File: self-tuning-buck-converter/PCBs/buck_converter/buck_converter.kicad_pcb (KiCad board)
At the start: 2 copper layers, 42 parts, among them Q1 NMOS, U1 AMP from lab, U2 LM7322, U3 LT1999-50, U4 LD1117V50, U6 ESP32-DEVKITC-32D, U7 IR2125, U8 MAX11644

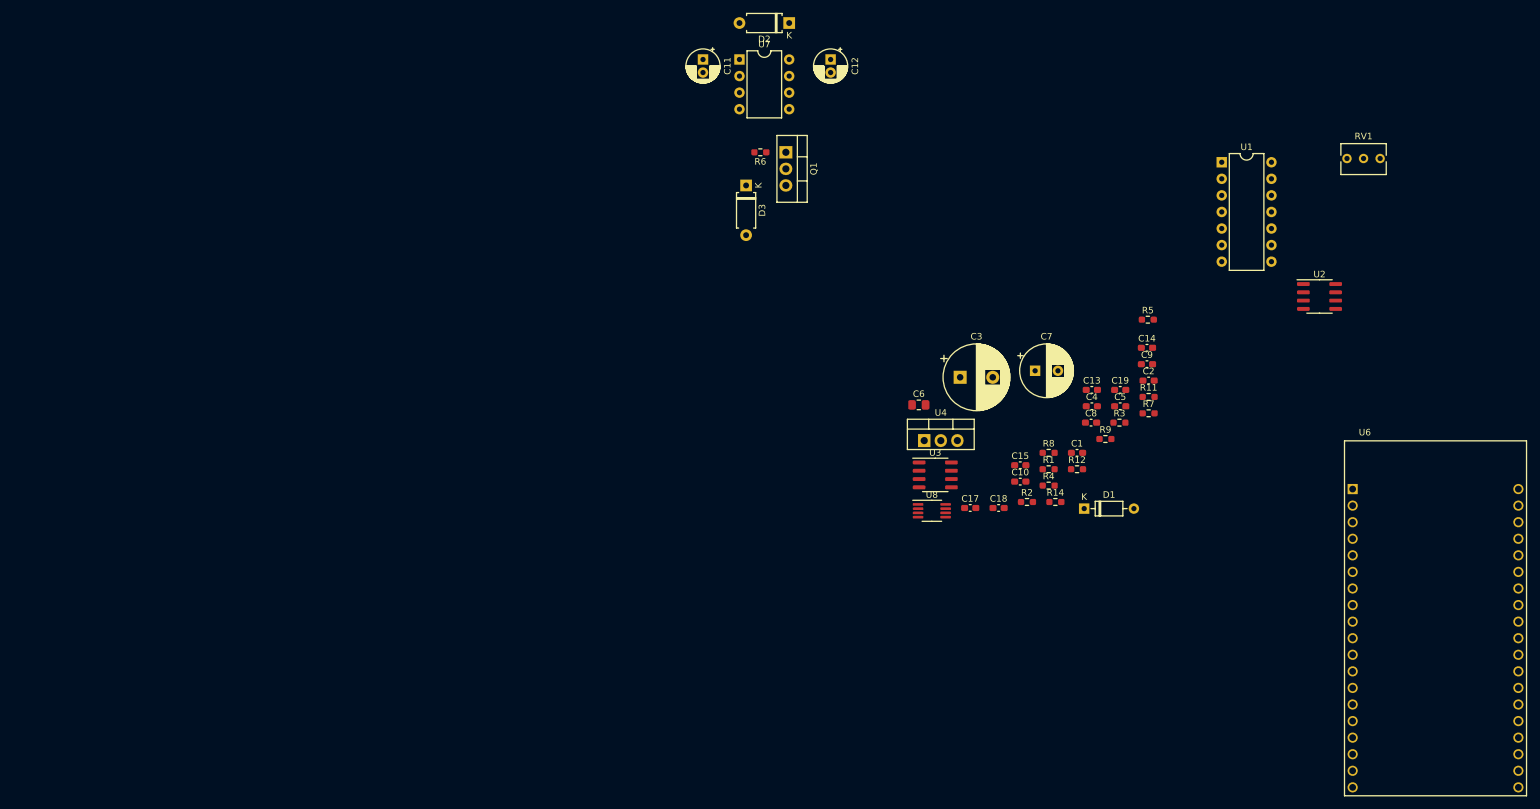
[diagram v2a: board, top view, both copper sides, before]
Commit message: begin and almost complete the PCB design of the buck converter:
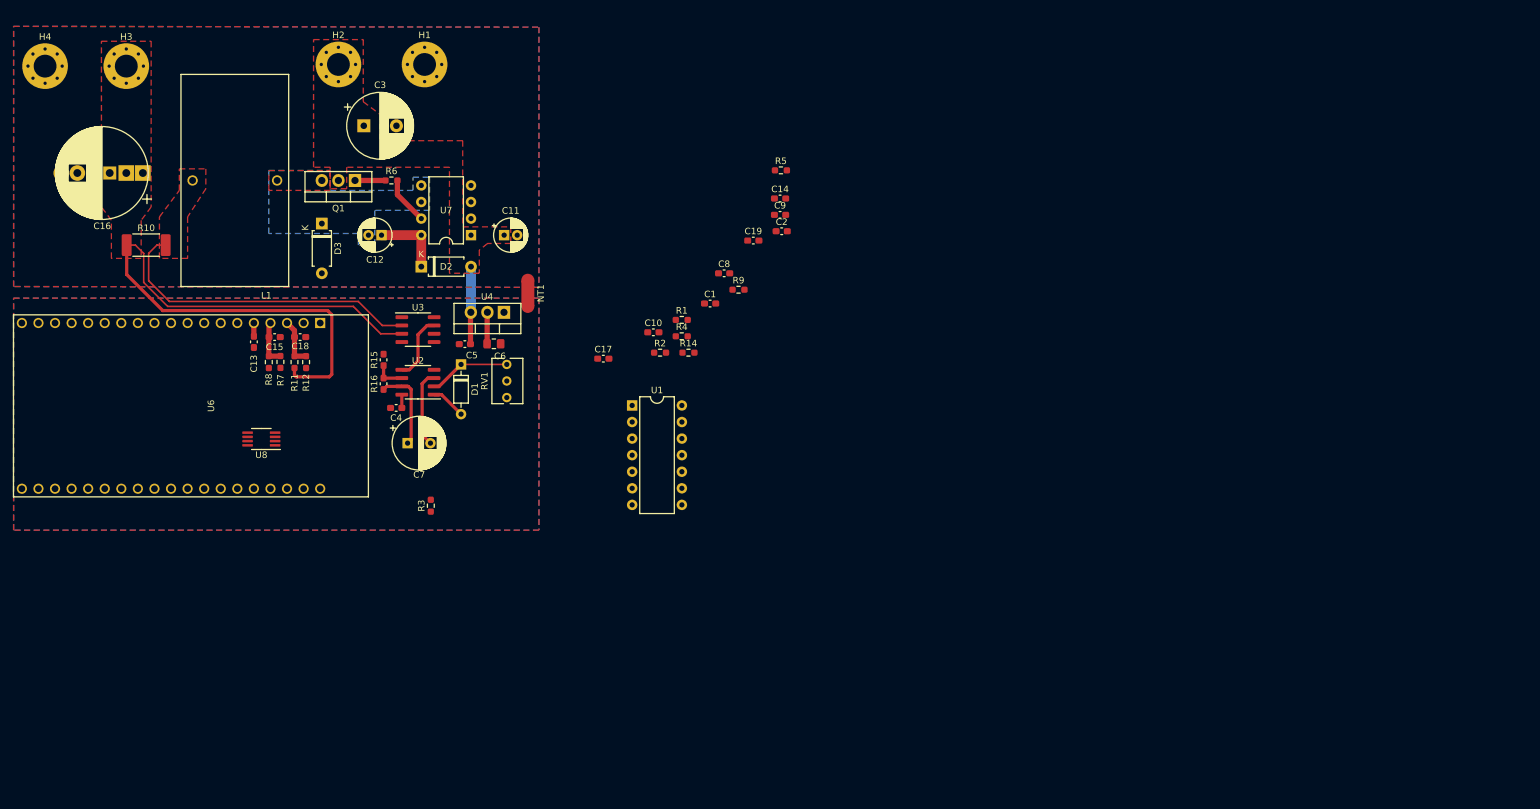
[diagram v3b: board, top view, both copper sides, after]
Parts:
- added C16: 470u 50V, multi_capacitor:multi_cap, F.Cu at (-204.3, -111.5)
- added H1: GND_IN, MountingHole:MountingHole_3.5mm_Pad_Via, F.Cu at (-154.9, -128.0)
- added H2: VCC_IN, MountingHole:MountingHole_3.5mm_Pad_Via, F.Cu at (-168.1, -128.0)
- added H3: LOAD +, MountingHole:MountingHole_3.5mm_Pad_Via, F.Cu at (-200.7, -127.8)
- added H4: LOAD -, MountingHole:MountingHole_3.5mm_Pad_Via, F.Cu at (-213.1, -127.8)
- added L1: L, IND_HCTI-150-5.0:IND_HCTI-150-5.0, F.Cu at (-184.0, -110.2)
- added NT1: Net-Tie_2, NetTie:NetTie-2_SMD_Pad2.0mm, F.Cu at (-139.1, -92.9)
- added R10: 60m, Resistor_SMD:R_2512_6332Metric_Pad1.52x3.35mm_HandSolder, F.Cu at (-197.6, -100.3)
- added R15: 10k, Resistor_SMD:R_0603_1608Metric_Pad1.05x0.95mm_HandSolder, F.Cu at (-161.2, -82.7)
- added R16: 10k, Resistor_SMD:R_0603_1608Metric_Pad1.05x0.95mm_HandSolder, F.Cu at (-161.2, -79.1)
- U2: value LM7322 -> OPA2830
- moved U6 193.5 mm to (-190.7, -75.7), turned to 270 degrees
- moved U2 138.8 mm to (-156.0, -79.3), turned to 180 degrees
- moved RV1 137.5 mm to (-142.3, -82.0), turned to 90 degrees
- moved R7 133.3 mm to (-177.0, -82.4), turned to 90 degrees
- moved R11 131.0 mm to (-174.9, -82.4), turned to 90 degrees
- moved C13 128.6 mm to (-181.1, -85.5), turned to 90 degrees
- moved R8 120.3 mm to (-178.8, -82.4), turned to 270 degrees
- moved R12 119.3 mm to (-173.1, -82.4), turned to 270 degrees
- moved C15 116.0 mm to (-177.9, -86.2), turned to 180 degrees
- moved C18 110.2 mm to (-174.0, -86.2), turned to 180 degrees
- moved C4 106.6 mm to (-159.3, -75.4)
- moved R3 106.3 mm to (-154.0, -60.4), turned to 90 degrees
- moved U8 103.4 mm to (-180.0, -70.6), turned to 180 degrees
- moved C5 100.9 mm to (-148.8, -85.2), turned to 180 degrees
- moved C3 99.2 mm to (-164.3, -118.6)
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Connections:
- C7 pad 1: Sense_out -> Sense_ripple
- R5 pad 2: Sense_out -> Sense_avg
- RV1 pad 3: Net-(RV1-Pad3) -> (no net)
- U1 pad 2: Net-(R1-Pad2) -> V_ref
- U1 pad 3: V_ref -> Net-(R1-Pad2)
- U1 pad 5: Pk_voltage -> Net-(C9-Pad2)
- U1 pad 6: Net-(C9-Pad2) -> Pk_voltage
- U2 pad 5: (no net) -> Sense_avg
- U2 pad 6: (no net) -> Net-(R15-Pad1)
- U2 pad 7: (no net) -> Sense_ripple
- U3 pad 7: Sense_out -> Sense_avg
- U3 pad 8: Net-(U3-Pad8) -> (no net)
- U6 pad 1: Net-(U6-Pad1) -> (no net)
- U6 pad 12: Net-(U6-Pad12) -> (no net)
- U6 pad 13: Net-(U6-Pad13) -> (no net)
- U6 pad 15: Net-(U6-Pad15) -> (no net)
- U6 pad 16: Net-(U6-Pad16) -> (no net)
- U6 pad 17: Net-(U6-Pad17) -> (no net)
- U6 pad 18: Net-(U6-Pad18) -> (no net)
- U6 pad 2: Net-(U6-Pad2) -> (no net)
- U6 pad 21: Net-(U6-Pad21) -> (no net)
- U6 pad 22: Net-(U6-Pad22) -> (no net)
- U6 pad 23: Net-(U6-Pad23) -> (no net)
- U6 pad 24: Net-(U6-Pad24) -> (no net)
- U6 pad 25: Net-(U6-Pad25) -> (no net)
- U6 pad 27: Net-(U6-Pad27) -> (no net)
- U6 pad 28: Net-(U6-Pad28) -> (no net)
- U6 pad 29: Net-(U6-Pad29) -> (no net)
- U6 pad 30: Net-(U6-Pad30) -> (no net)
- U6 pad 31: Net-(U6-Pad31) -> (no net)
- U6 pad 32: Net-(U6-Pad32) -> (no net)
- U6 pad 33: Net-(U6-Pad33) -> (no net)
- U6 pad 34: Net-(U6-Pad34) -> (no net)
- U6 pad 35: Net-(U6-Pad35) -> (no net)
- U6 pad 36: Net-(U6-Pad36) -> (no net)
- U6 pad 37: Net-(U6-Pad37) -> (no net)
- U6 pad 38: Net-(U6-Pad38) -> (no net)
- U6 pad 6: Net-(U6-Pad6) -> (no net)
- U6 pad 7: Net-(U6-Pad7) -> (no net)
- U6 pad 8: Net-(U6-Pad8) -> (no net)
- U7 pad 3: Net-(U7-Pad3) -> (no net)
- U8 pad 3: Net-(U8-Pad3) -> (no net)
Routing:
- net V_load: track 0.00 -> 105.1 mm
- net /sen_p: track 0.00 -> 49.0 mm
- net +12V: track 0.00 -> 13.9 mm
- net Sense_ripple: track 0.00 -> 13.1 mm
- net Net-(D1-Pad1): track 0.00 -> 12.5 mm
- net Net-(C7-Pad2): track 0.00 -> 11.8 mm
- net Net-(C12-Pad1): track 0.00 -> 10.9 mm
- net Sense_avg: track 0.00 -> 10.1 mm
- net load_sense: track 0.00 -> 7.40 mm
- net Net-(R6-Pad2): track 0.00 -> 7.36 mm
- net V_supply: track 0.00 -> 6.97 mm
- net Net-(D1-Pad2): track 0.00 -> 5.37 mm
- net +5V: track 0.00 -> 4.84 mm
- net Net-(R15-Pad1): track 0.00 -> 4.71 mm
- net Net-(Q1-Pad1): track 0.00 -> 4.68 mm
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- added copper zone on F.Cu, net +12V
- added copper zone on F.Cu, net /sen_p
- added copper zone on B.Cu, net GND
- added copper zone on F.Cu, net GND
- added copper zone on B.Cu, net GNDD
- added copper zone on F.Cu, net GNDD
- added copper zone on B.Cu, net Net-(C12-Pad2)
- added copper zone on F.Cu, net Net-(C12-Pad2)
- added copper zone on F.Cu, net V_load

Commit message: completed the PCB design
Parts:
- added R13: 16k, Resistor_SMD:R_0603_1608Metric_Pad0.98x0.95mm_HandSolder, F.Cu at (-194.2, -87.7)
- C8: value 0.1u 16V -> 1u 16V
- IN +: renamed from H2
- IN -: renamed from H1
- OUT  -: renamed from H4
- OUT +: renamed from H3
- U1: value AMP from lab -> TLO84CN
- moved C2 106.9 mm to (-205.7, -85.1), turned to 270 degrees
- moved R5 105.2 mm to (-201.7, -83.8), turned to 270 degrees
- moved C14 103.4 mm to (-192.6, -60.6), turned to 90 degrees
- moved C9 100.5 mm to (-196.5, -75.6), turned to 90 degrees
- moved R9 90.2 mm to (-190.9, -60.7), turned to 270 degrees
- moved C8 87.2 mm to (-195.8, -87.7), turned to 90 degrees
- moved C19 87.0 mm to (-184.0, -65.4), turned to 270 degrees
- moved C10 80.0 mm to (-199.8, -83.8), turned to 90 degrees
- moved R4 79.9 mm to (-194.7, -75.6), turned to 90 degrees
- moved R1 79.6 mm to (-194.7, -80.7), turned to 90 degrees
- moved R2 77.6 mm to (-196.4, -80.7), turned to 270 degrees
- moved C1 72.4 mm to (-182.7, -79.9), turned to 270 degrees
- moved R14 72.1 mm to (-184.8, -68.0), turned to 180 degrees
- moved U1 70.0 mm to (-192.2, -86.7)
- moved C17 60.8 mm to (-185.7, -65.4), turned to 270 degrees
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- renumbered L1 to INDUCTOR
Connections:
- R8 pad 2: GND -> GNDD
- RV1 pad 3: (no net) -> Net-(RV1-Pad3)
- U1 pad 1: V_ref -> Net-(R13-Pad2)
- U1 pad 2: V_ref -> Net-(R13-Pad2)
- U3 pad 8: (no net) -> Net-(U3-Pad8)
- U6 pad 1: (no net) -> Net-(U6-Pad1)
- U6 pad 10: SCL -> SDA
- U6 pad 12: (no net) -> Net-(U6-Pad12)
- U6 pad 13: (no net) -> Net-(U6-Pad13)
- U6 pad 15: (no net) -> Net-(U6-Pad15)
- U6 pad 16: (no net) -> Net-(U6-Pad16)
- U6 pad 17: (no net) -> Net-(U6-Pad17)
- U6 pad 18: (no net) -> Net-(U6-Pad18)
- U6 pad 2: (no net) -> Net-(U6-Pad2)
- U6 pad 21: (no net) -> Net-(U6-Pad21)
- U6 pad 22: (no net) -> Net-(U6-Pad22)
- U6 pad 23: (no net) -> Net-(U6-Pad23)
- U6 pad 24: (no net) -> Net-(U6-Pad24)
- U6 pad 25: (no net) -> Net-(U6-Pad25)
- U6 pad 27: (no net) -> Net-(U6-Pad27)
- U6 pad 28: (no net) -> Net-(U6-Pad28)
- U6 pad 29: (no net) -> Net-(U6-Pad29)
- U6 pad 30: (no net) -> Net-(U6-Pad30)
- U6 pad 31: (no net) -> Net-(U6-Pad31)
- U6 pad 32: (no net) -> Net-(U6-Pad32)
- U6 pad 33: (no net) -> Net-(U6-Pad33)
- U6 pad 34: (no net) -> Net-(U6-Pad34)
- U6 pad 35: (no net) -> Net-(U6-Pad35)
- U6 pad 36: (no net) -> Net-(U6-Pad36)
- U6 pad 37: (no net) -> Net-(U6-Pad37)
- U6 pad 38: (no net) -> Net-(U6-Pad38)
- U6 pad 6: (no net) -> Net-(U6-Pad6)
- U6 pad 7: (no net) -> Net-(U6-Pad7)
- U6 pad 8: (no net) -> Net-(U6-Pad8)
- U6 pad 9: SDA -> SCL
- U7 pad 3: (no net) -> Net-(U7-Pad3)
- U8 pad 3: (no net) -> Net-(U8-Pad3)
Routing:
- net +5V: track 4.84 -> 139.7 mm, vias 0 -> 2
- net +12V: track 13.9 -> 125.7 mm, vias 0 -> 3
- net V_load: track 105.1 -> 25.7 mm
- net PWM: track 0.00 -> 63.8 mm
- net load_sense: track 7.40 -> 71.1 mm, vias 0 -> 2
- net Avg_voltage: track 2.05 -> 54.2 mm, vias 0 -> 1
- net V_ref: track 0.00 -> 40.0 mm, vias 0 -> 2
- net SDA: track 0.00 -> 37.1 mm
- net SCL: track 0.00 -> 34.2 mm
- net /sen_p: track 49.0 -> 21.3 mm
- net Pk_voltage: track 0.00 -> 8.86 mm
- net Net-(C9-Pad2): track 0.00 -> 8.59 mm
- net GND: track 0.00 -> 5.81 mm
- net Net-(C7-Pad2): track 11.8 -> 17.5 mm
- net GNDD: track 0.00 -> 5.37 mm, vias 0 -> 61
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- added copper zone on F.Cu, net +5V
- added copper zone on F.Cu, net Net-(C17-Pad1)
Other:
- board outline added: 91.2 x 82.6 mm

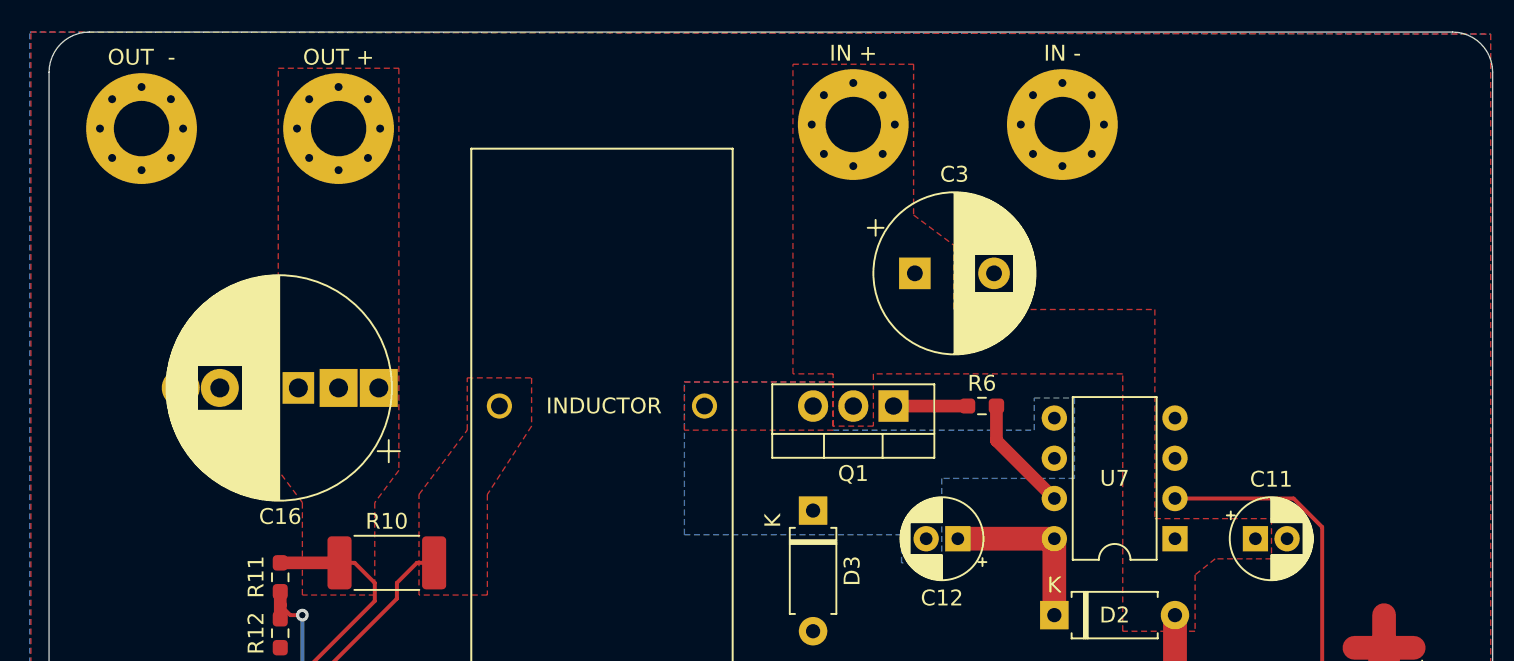
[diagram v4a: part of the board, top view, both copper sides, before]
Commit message: added via stitching to the board
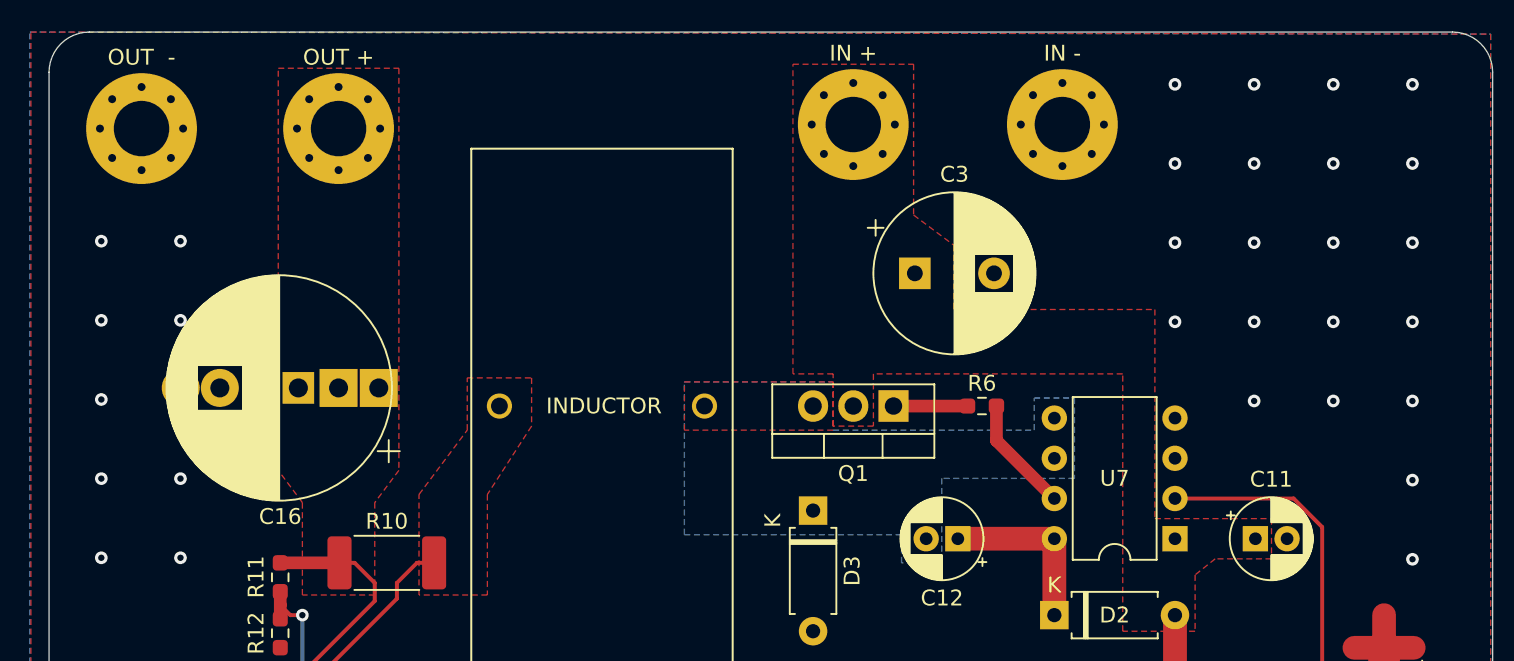
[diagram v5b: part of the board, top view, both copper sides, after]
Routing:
- net GND: vias 0 -> 30

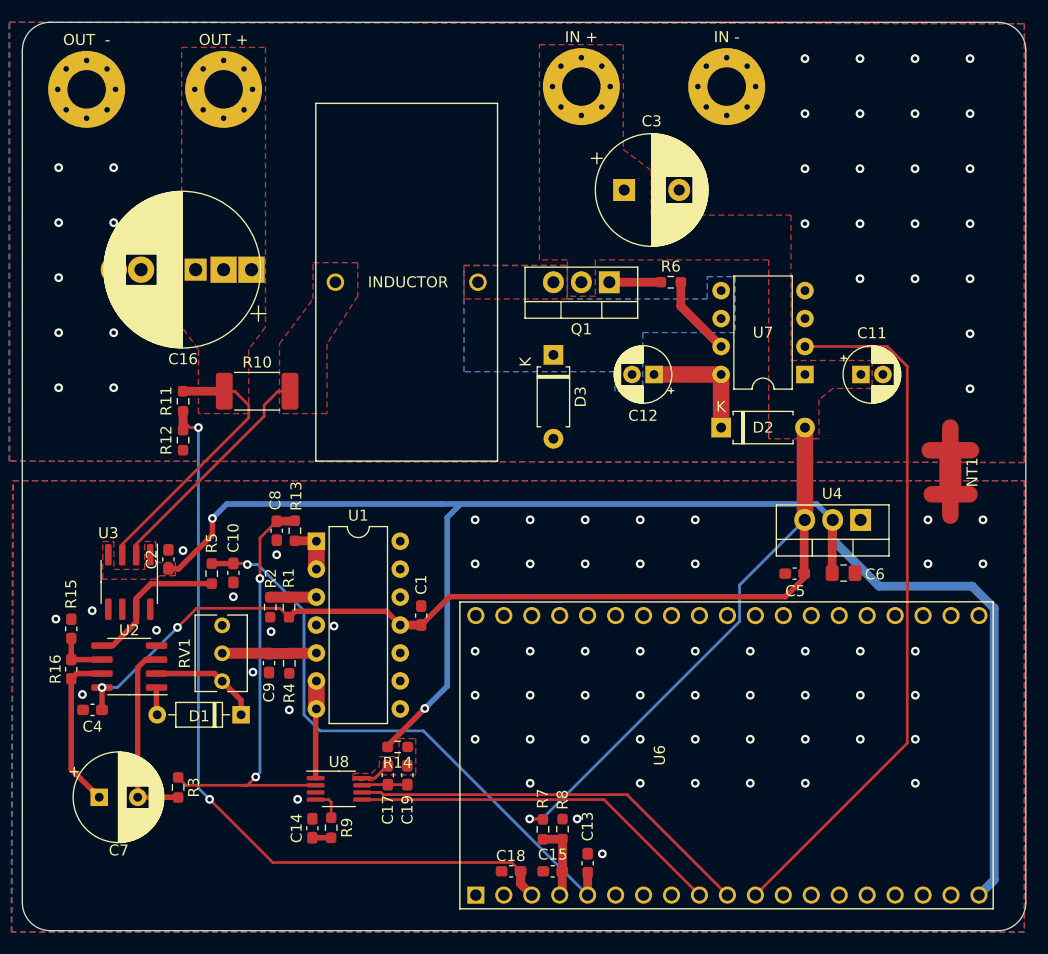
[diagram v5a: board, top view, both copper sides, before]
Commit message: update PCB, and create the iBOM
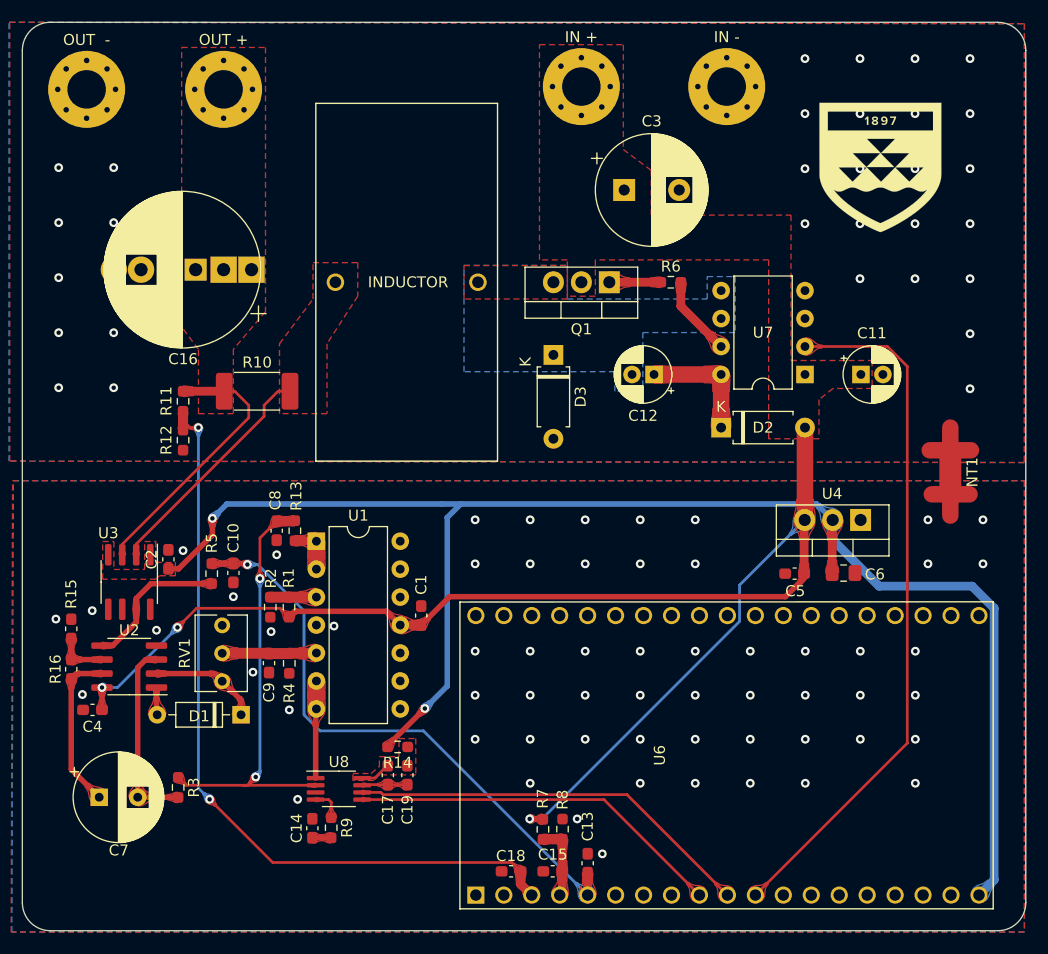
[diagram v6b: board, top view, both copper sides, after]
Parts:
- added G***: LOGO, graphic:logo, F.Cu at (-141.0, -120.7)
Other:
- board text added: "Self Tuning Buck Converter Rev 1 Niels Clayton"
